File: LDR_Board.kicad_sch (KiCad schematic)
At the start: 23 parts, among them J1 Conn_01x07_Pin, J2 Conn_01x02_Pin

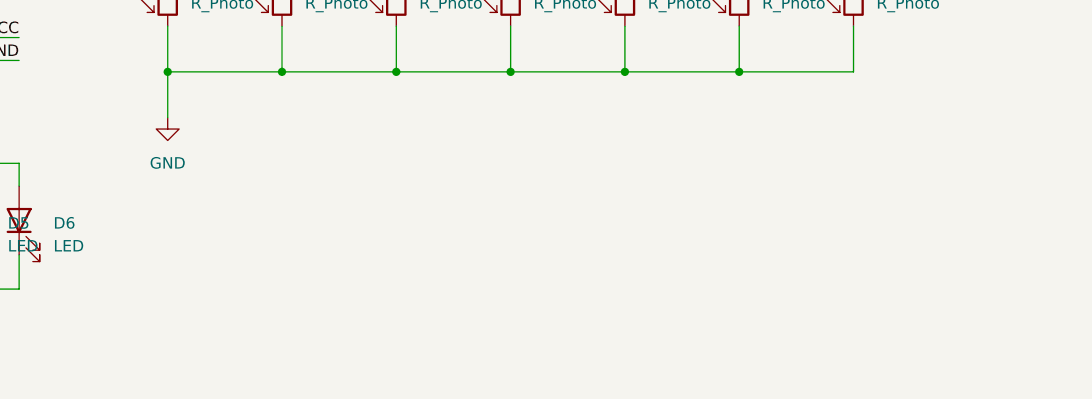
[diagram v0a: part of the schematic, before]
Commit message: Routed traces and added silkscreen
Still need to export for manufacturing, but initial design is complete.
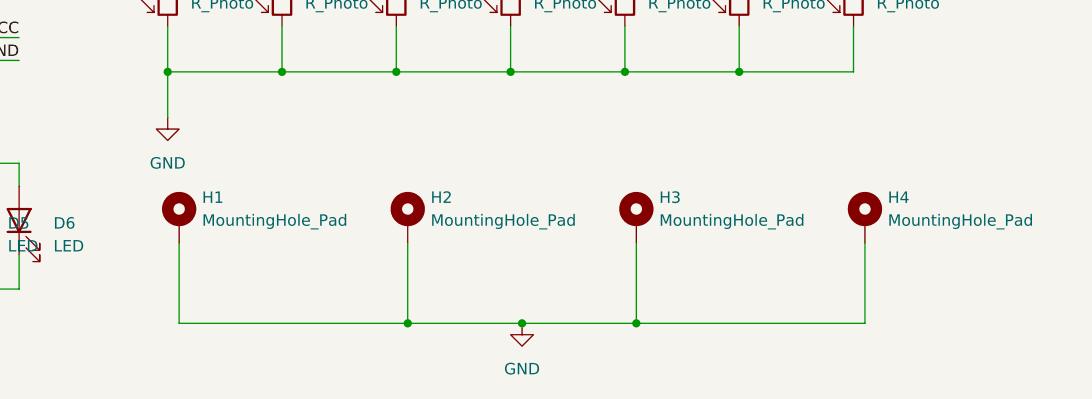
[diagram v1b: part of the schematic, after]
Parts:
- added H1, H2, H3, H4: MountingHole_Pad, MountingHole:MountingHole_3.2mm_M3_Pad, symbol Mechanical:MountingHole_Pad
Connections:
- net GND: now also H1.1, H2.1, H3.1, H4.1
